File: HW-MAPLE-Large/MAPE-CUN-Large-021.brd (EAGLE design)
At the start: 100 x 87.3 mm, 71 parts, among them X1 SMA, X2 SMA, X3 SMA, X4 SMA, X5 SMA, X6 SMA

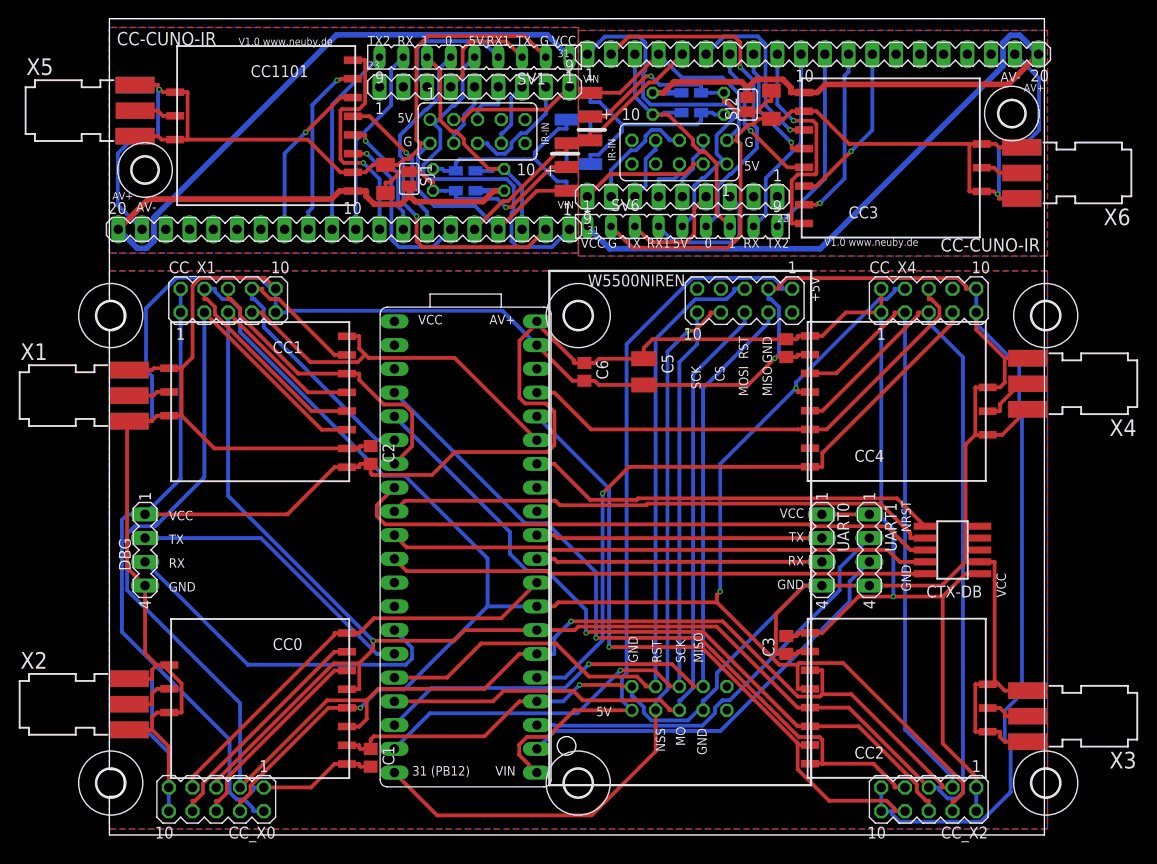
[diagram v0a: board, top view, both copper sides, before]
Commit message: Fix Large-PCB; Adapter for Stamps
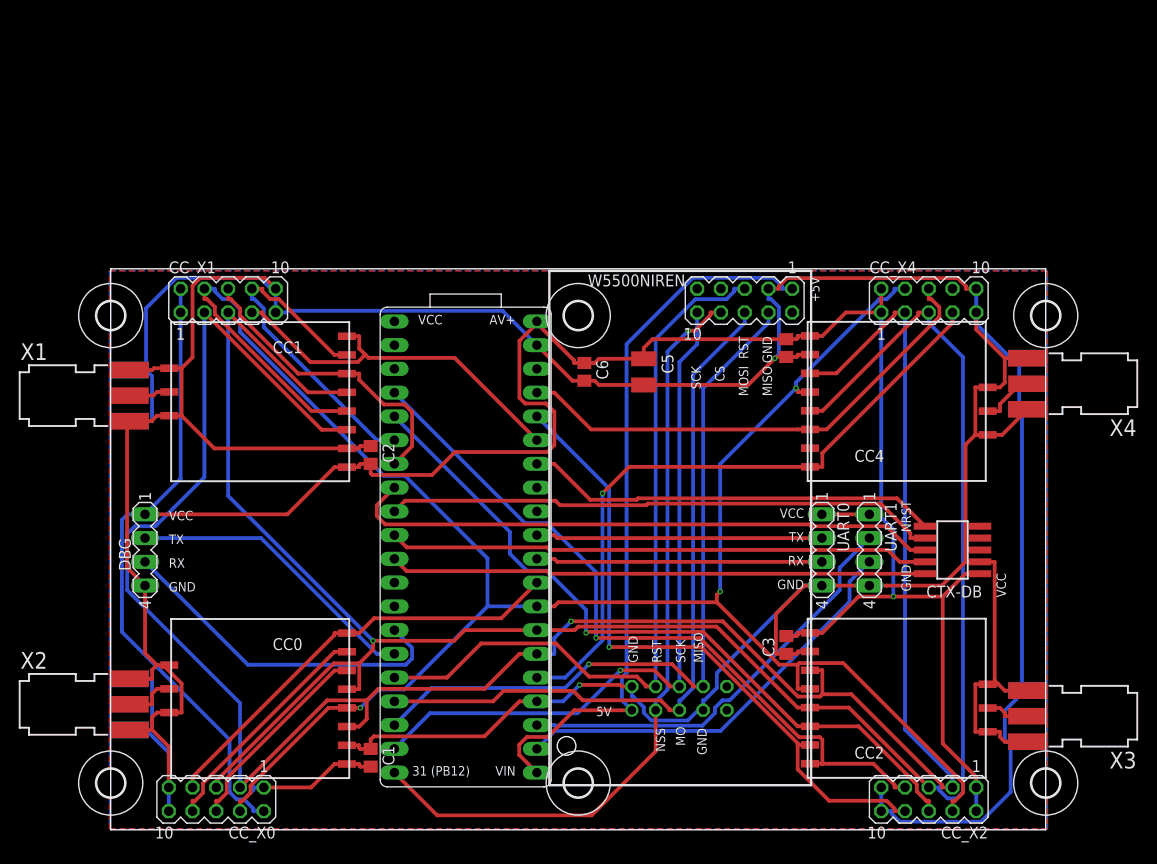
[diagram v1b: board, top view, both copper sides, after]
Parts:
- removed C7, C8: 4,7uF, rcl:C1206K
- removed CC1101, CC3: CC1101_MODULE1SMD, wireless:CC1101_MODULE1_SMD
- removed GND, GND1, IR+, IR+1, IR-IN, IR-IN1, PC+, PC+1, PC-, PC-1, PWR+, PWR+1, PWR-, PWR-1: (no value), wirepad:SMD1,27-2,54
- removed H7, H8: MOUNT-HOLE2.8, holes:2,8
- removed R1, R2: 100, rcl:0204/7
- removed R3, R4: 100, rcl:R0805W
- removed R5, R6: 220, rcl:0204/7
- removed R7, R8: 220, rcl:R0805W
- removed SJ1, SJ2: (no value), jumper:SJ
- removed SV1, SV6: (no value), con-lsta:FE09
- removed SV2, SV4: (no value), con-lstb:MA20-1
- removed SV3, SV5: (no value), con-lstb:MA09-1
- removed W1, W2: (no value), con-lsta:FE05-2
- removed X5, X6: SMA, sma:SMA
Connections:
- removed net +5V1: SV1.5, SV4.1, W1.1
- removed net +5V2: SV2.1, SV6.5, W2.1
- removed net 0-PB1: SV2.2, SV6.6
- removed net 0-PB11: SV1.6, SV4.2
- removed net 1: SV2.17
- removed net 1-PB1: R6.1, R8.1, SV2.3, SV6.7
- removed net 1-PB10: R5.1, R7.1, SV1.7, SV4.3
- removed net 12: SV4.15
- removed net 13: SV4.16
- removed net 14: SV4.17
- removed net 2: SV2.16
- removed net 3: SV2.15
- removed net 3-PB0: IR-IN.1, SV4.5
- removed net 3-PB1: IR-IN1.1, SV2.5
- removed net CC_IN0: U$1.33
- removed net CC_IN_4: CC1101.GDO2, SV4.13
- removed net CC_IN_5: CC3.GDO2, SV2.13
- removed net CC_OUT0: U$1.32
- removed net CC_OUT_3: CC1101.GDO0, SV4.12
- removed net CC_OUT_4: CC3.GDO0, SV2.12
- removed net CSN: CC1101.CSN, SV4.9
- removed net CSN1: CC3.CSN, SV2.9
- removed net GND1: C7.2, CC1101.GND@0, CC1101.GND@1, CC1101.GND@2, GND.1, SV1.2, SV4.19, SV4.4, W1.2, X5.GND@1, X5.GND@2, X5.GND@3, X5.GND@4
- removed net GND2: C8.2, CC3.GND@0, CC3.GND@1, CC3.GND@2, GND1.1, SV2.19, SV2.4, SV6.2, W2.2, X6.GND@1, X6.GND@2, X6.GND@3, X6.GND@4
- removed net IR+: C7.1, IR+.1, R2.1, R3.1, SJ1.1
- removed net IR+1: C8.1, IR+1.1, R1.1, R4.1, SJ2.1
- removed net MISO3: SV5.7, W1.8
- removed net MISO4: SV3.7, W2.8
- removed net MOSI: CC1101.MOSI, SV4.6
- removed net MOSI2: SV5.6, W1.5
- removed net MOSI3: CC3.MOSI, SV2.6
- removed net MOSI4: SV3.6, W2.5
- removed net N$10: CC3.MISO, SV2.7
- removed net N$11: CC3.SCLK, SV2.8
- removed net N$5: CC1101.ANT, X5.1
- removed net N$6: CC1101.MISO, SV4.7
- removed net N$7: CC1101.SCLK, SV4.8
- removed net N$9: CC3.ANT, X6.1
- removed net PWR+: PC+.1, PWR+.1, R5.2, R7.2
- removed net PWR+1: PC+1.1, PWR+1.1, R6.2, R8.2
- removed net PWR-: PC-.1, PWR-.1
- removed net PWR-1: PC-1.1, PWR-1.1
- removed net RX2: SV1.4, SV5.3
- removed net RX3: SV3.3, SV6.4
- removed net S2RX: SV1.8, SV4.10
- removed net S2RX1: SV2.10, SV6.8
- removed net S2TX: SV1.9, SV4.11
- removed net S2TX1: SV2.11, SV6.9
- removed net SCK3: SV5.8, W1.6
- removed net SCK4: SV3.8, W2.6
- removed net TX2: SV1.3, SV5.4
- removed net TX3: SV3.4, SV6.3
- removed net USB-DM: SV5.1
- removed net USB-DM1: SV3.1
- removed net USB-DP: SV5.2
- removed net USB-DP1: SV3.2
- removed net VCC1: CC1101.VCC, R2.2, R3.2, SJ1.2, SV1.1, SV4.20
- removed net VCC2: CC3.VCC, R1.2, R4.2, SJ2.2, SV2.20, SV6.1
- removed net WIZ_CS1: SV5.9, W1.3
- removed net WIZ_CS2: SV3.9, W2.3
- removed net WIZ_RST1: SV5.5, W1.4
- removed net WIZ_RST2: SV3.5, W2.4
- net CC_IN_0: now also U$1.33
- net CC_OUT_0: now also U$1.32
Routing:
- net GND2: track 118.7 -> 0.00 mm, vias 1 -> 0
- net GND1: track 118.7 -> 0.00 mm, vias 1 -> 0
- net VCC1: track 110.1 -> 0.00 mm
- net VCC2: track 110.1 -> 0.00 mm
- net +5V2: track 39.4 -> 0.00 mm
- net +5V1: track 39.4 -> 0.00 mm
- net 0-PB11: track 37.6 -> 0.00 mm, vias 1 -> 0
- net 0-PB1: track 37.6 -> 0.00 mm, vias 1 -> 0
- net 1-PB10: track 27.1 -> 0.00 mm
- net 1-PB1: track 27.1 -> 0.00 mm
- net IR+: track 25.5 -> 0.00 mm, vias 1 -> 0
- net IR+1: track 25.5 -> 0.00 mm, vias 1 -> 0
- net CSN: track 24.5 -> 0.00 mm, vias 1 -> 0
- net CSN1: track 24.5 -> 0.00 mm, vias 1 -> 0
- net PWR+: track 23.5 -> 0.00 mm
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- removed copper zone on layer 1, net GND1
- removed copper zone on layer 16, net GND1
- removed copper zone on layer 1, net GND2
- removed copper zone on layer 16, net GND2
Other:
- board size 100 x 87.3 mm -> 100 x 60 mm
- board text removed: "+"
- board text removed: "-"
- board text removed: "0"
- board text removed: "1"
- board text removed: "23"
- board text removed: "31"
- board text removed: "AV-"
- board text removed: "CC-CUNO-IR"
- board text removed: "G"
- board text removed: "IR-IN"
- board text removed: "PC"
- board text removed: "RX1"
- board text removed: "SW"
- board text removed: "TX2"
- board text removed: "V1.0 www.neuby.de"
